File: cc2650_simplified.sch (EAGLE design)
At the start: 13 parts, among them IC4 CC2650MODAMOHR, U402 TPS62233DRY

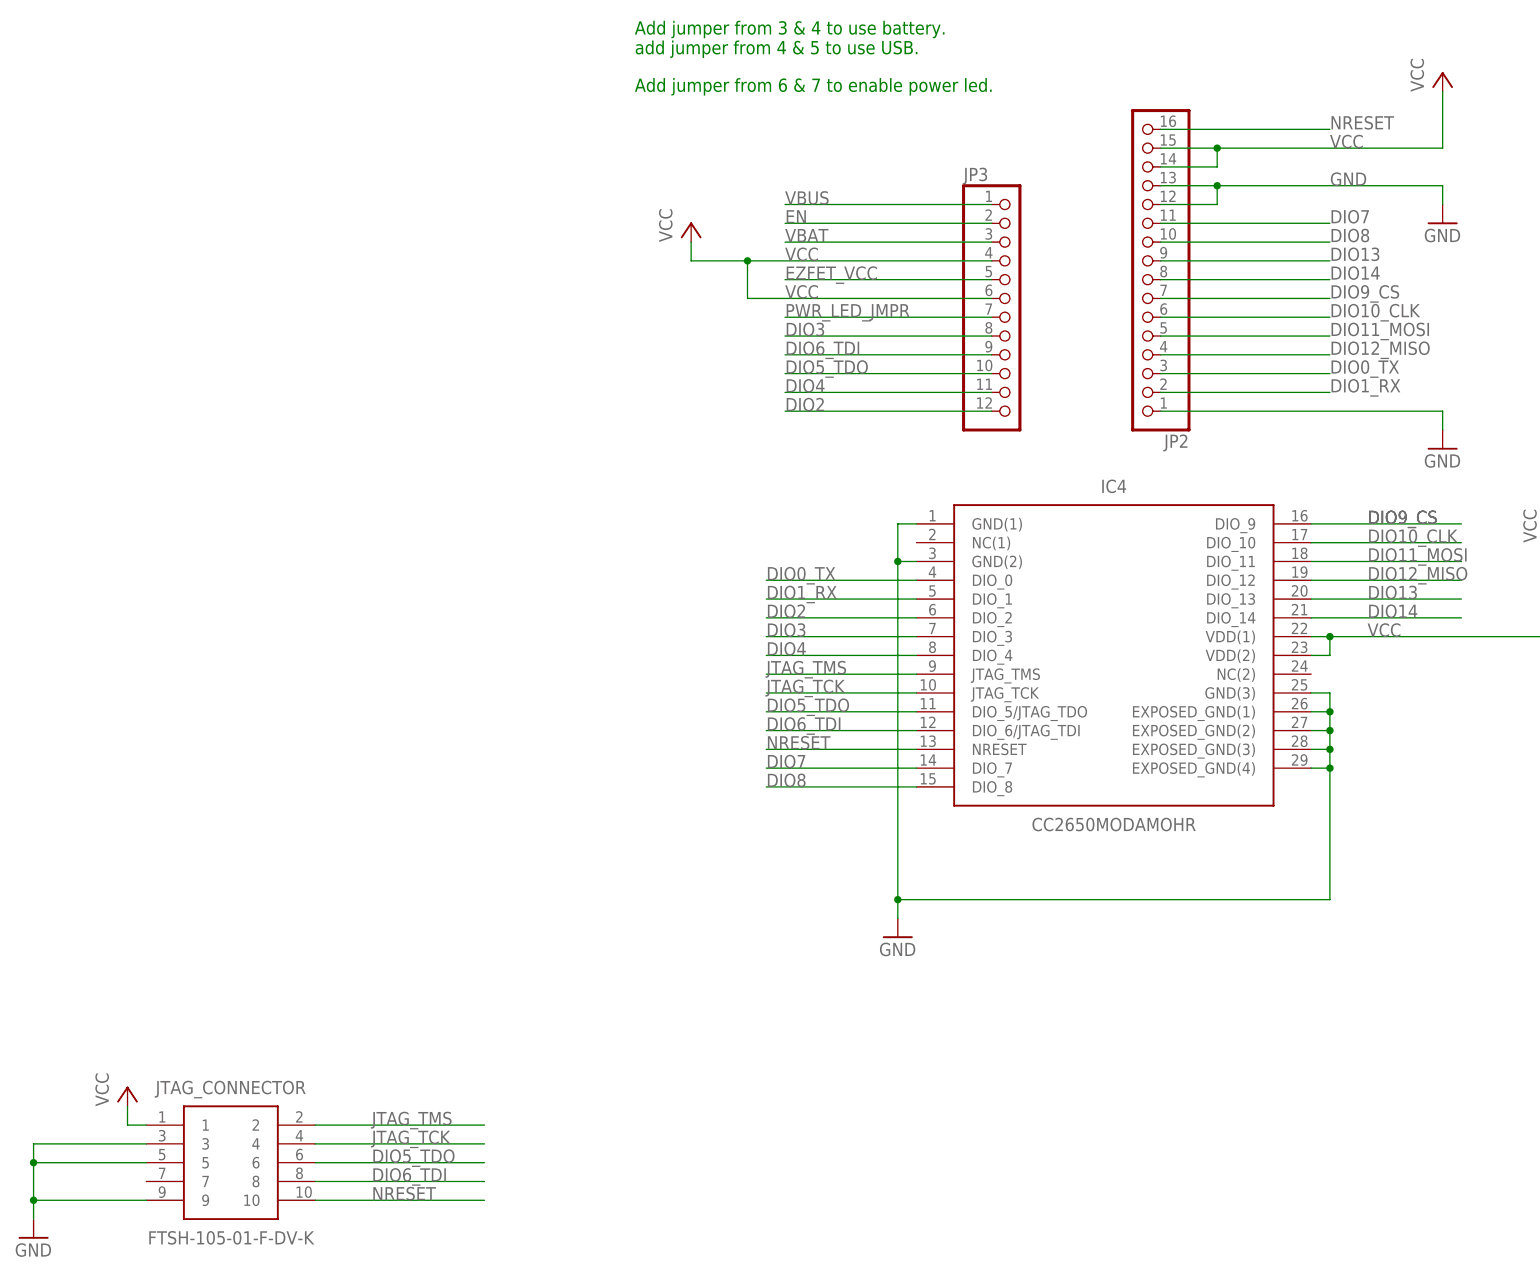
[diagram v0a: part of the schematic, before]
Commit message: Changed Voltage Regulator to 3.3V output.
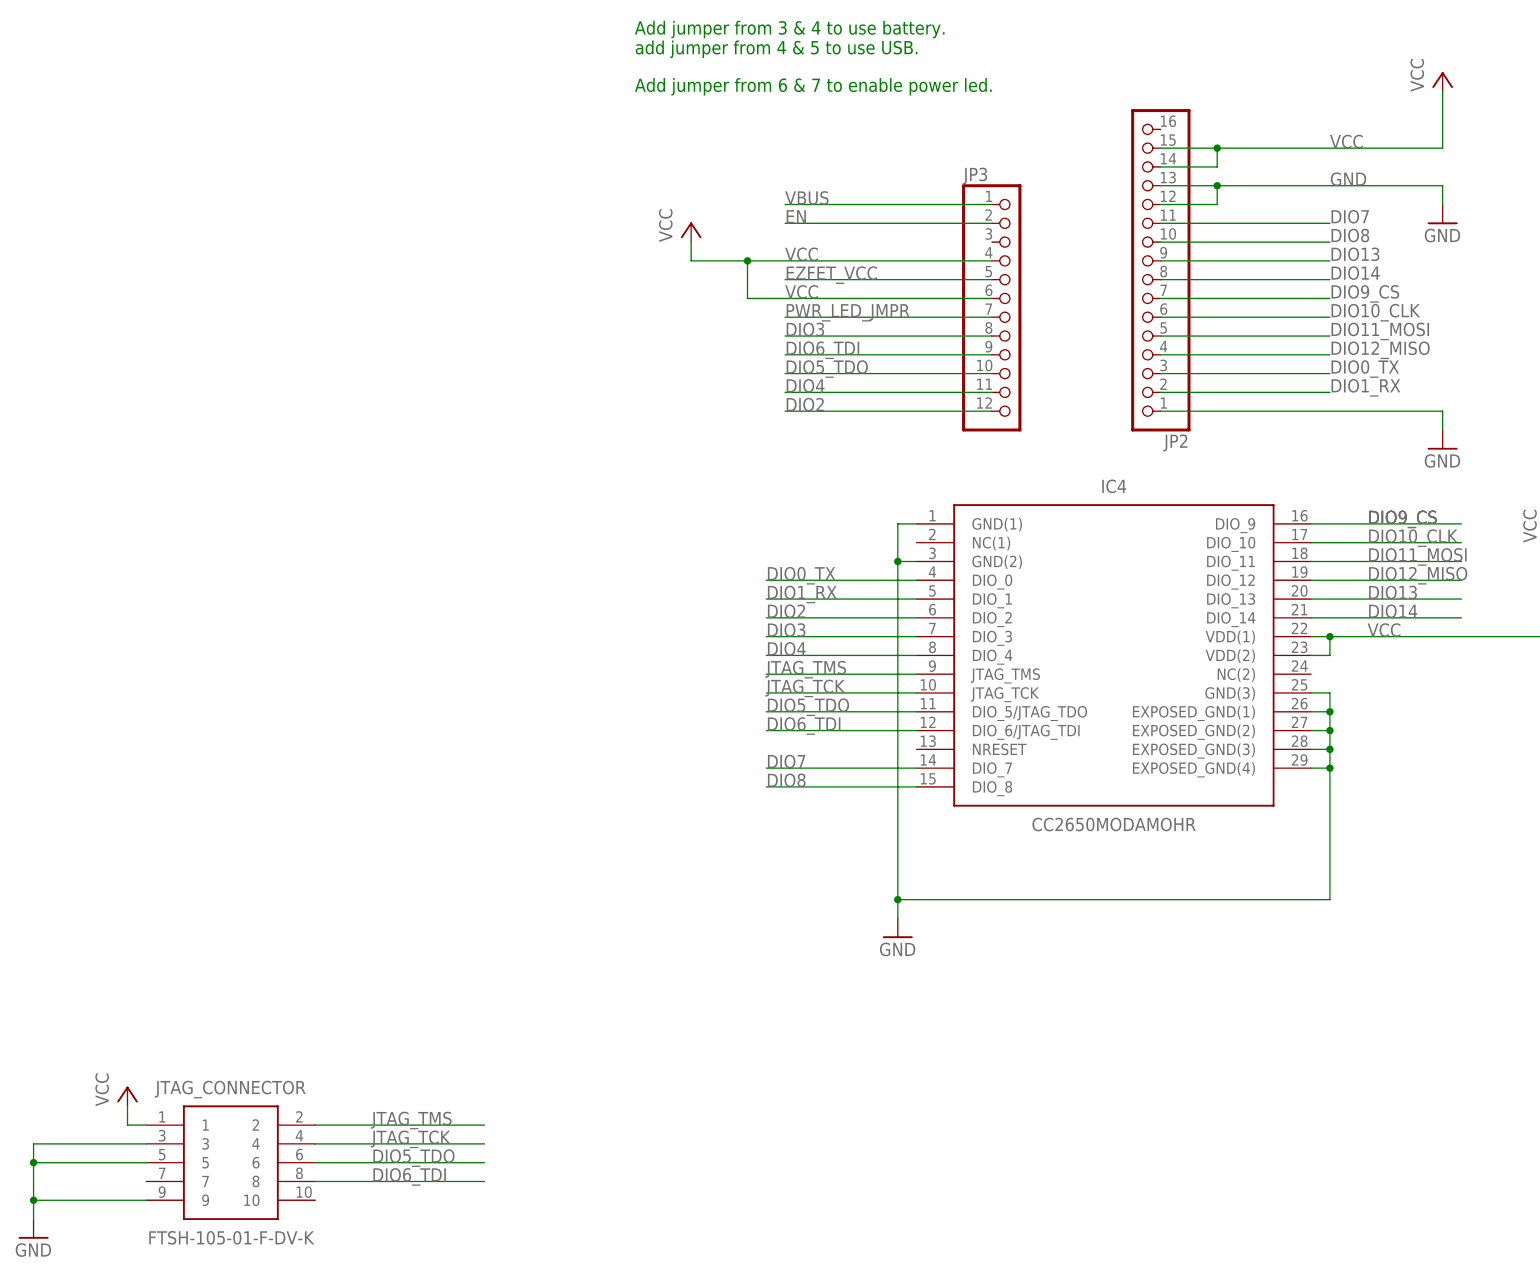
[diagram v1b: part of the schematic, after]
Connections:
- removed net NRESET: IC4.NRESET, JP2.16, JTAG_CONNECTOR.10
- removed net VBAT: JP3.3
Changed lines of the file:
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@@
-</segment>
-</net>
-<net name="NRESET" class="0">
-<segment>
-<pinref part="JTAG_CONNECTOR" gate="G$1" pin="10"/>
-<wire x1="-185.42" y1="-83.82" x2="-162.56" y2="-83.82" width="0.1524" layer="91"/>
-<label x="-177.8" y="-83.82" size="1.778" layer="95"/>
-</segment>
-<segment>
-<pinref part="IC4" gate="G$1" pin="NRESET"/>
-<wire x1="-124.46" y1="-22.86" x2="-104.14" y2="-22.86" width="0.1524" layer="91"/>
-<label x="-124.46" y="-22.86" size="1.778" layer="95"/>
-</segment>
-<segment>
-<pinref part="JP2" gate="A" pin="16"/>
-<wire x1="-71.12" y1="60.96" x2="-48.26" y2="60.96" width="0.1524" layer="91"/>
-<label x="-48.26" y="60.96" size="1.778" layer="95"/>
 </segment>
 </net>
@@
 <segment>
 <wire x1="-210.82" y1="-71.12" x2="-210.82" y2="-73.66" width="0.1524" layer="91"/>
+<pinref part="P+3" gate="VCC" pin="VCC"/>
 <pinref part="JTAG_CONNECTOR" gate="G$1" pin="1"/>
-<wire x1="-210.82" y1="-73.66" x2="-208.28" y2="-73.66" width="0.1524" layer="91"/>
-<pinref part="P+3" gate="VCC" pin="VCC"/>
+<wire x1="-208.28" y1="-73.66" x2="-210.82" y2="-73.66" width="0.1524" layer="91"/>
 </segment>
 <segment>
@@
 </segment>
 </net>
-<net name="VBAT" class="0">
-<segment>
-<pinref part="JP3" gate="G$1" pin="3"/>
-<wire x1="-93.98" y1="45.72" x2="-121.92" y2="45.72" width="0.1524" layer="91"/>
-<label x="-121.92" y="45.72" size="1.778" layer="95"/>
-</segment>
-</net>
